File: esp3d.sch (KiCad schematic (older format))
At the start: 12 parts, among them J1 PROG, U1 LM1117-3.3, U2 ESP-12E

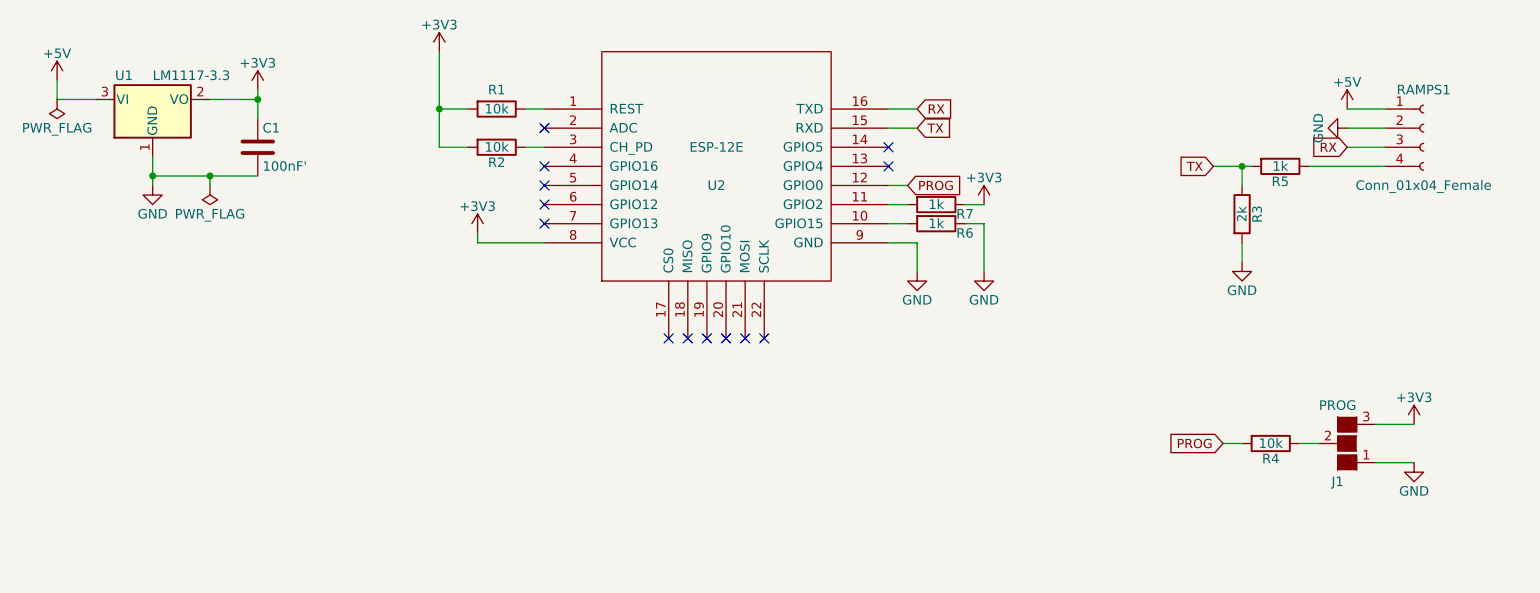
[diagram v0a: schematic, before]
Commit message: Reversed the ramps connector. Removed resistors that may have prevented programming
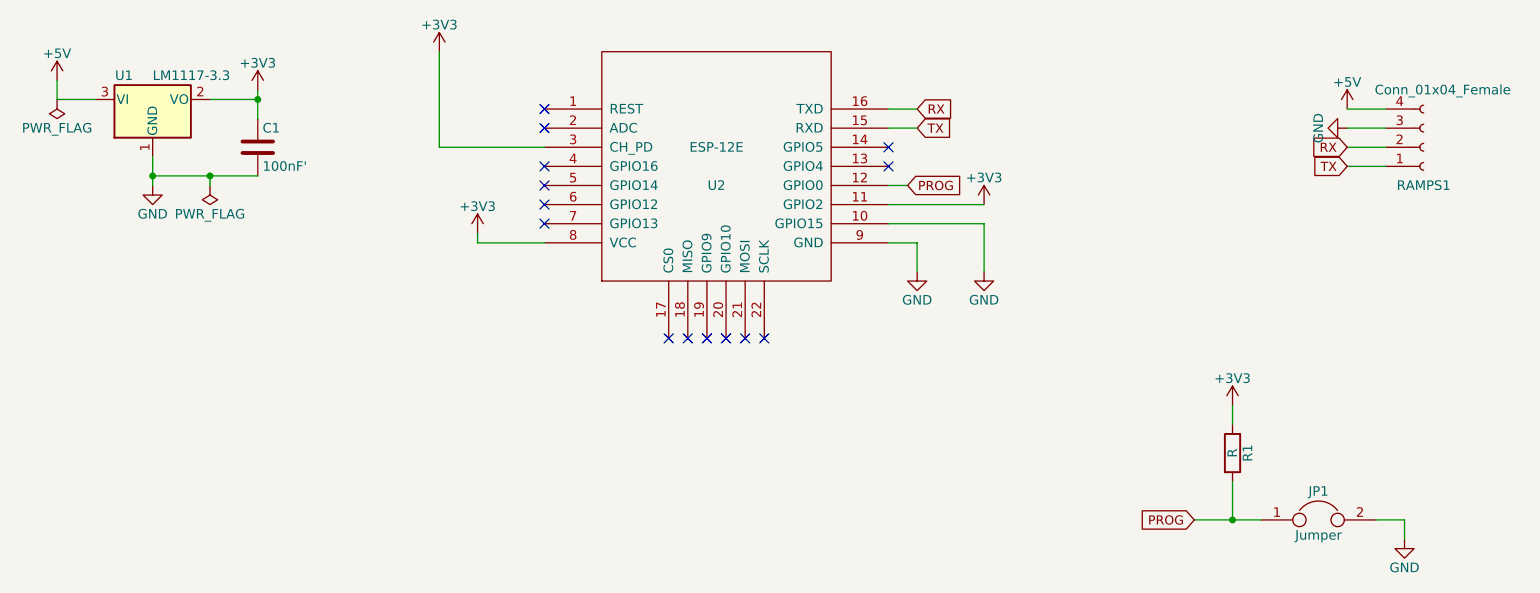
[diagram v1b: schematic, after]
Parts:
- removed J1: PROG, Connectors:GS3, symbol GS3
- removed R2, R4: 10k, Resistors_SMD:R_0805_HandSoldering, symbol R
- removed R3: 2k, Resistors_SMD:R_0805_HandSoldering, symbol R
- removed R5, R6, R7: 1k, Resistors_SMD:R_0805_HandSoldering, symbol R
- added JP1: Jumper, Resistors_Universal:Resistor_SMDuniversal_0805to2512_HandSoldering, symbol Jumper
- R1: value 10k -> R
- U2: footprint RF_Modules:ESP-12E -> ESP8266:ESP-12S_SMD
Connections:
- net +3V3: now also R1.1, U2.11 (GPIO2), U2.3 (CH_PD); no longer R1.2
- net +5V: now also RAMPS1.4 (Pin_4); no longer RAMPS1.1 (Pin_1)
- net GND: now also RAMPS1.3 (Pin_3), U2.10 (GPIO15), JP1.2; no longer RAMPS1.2 (Pin_2)
- net PROG: now also R1.2, JP1.1
- net RX: now also RAMPS1.2 (Pin_2); no longer RAMPS1.3 (Pin_3)
- net TX: now also RAMPS1.1 (Pin_1)
- net at U2.1 (REST): no longer R1.1
- no-connect marks 13 -> 14
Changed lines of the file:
@@
 LIBS:valves
 LIBS:ESP8266
+LIBS:esp3d-cache
 EELAYER 25 0
 EELAYER END
@@
 F 0 "U2" H 5850 3550 50  0000 C CNN
 F 1 "ESP-12E" H 5850 3750 50  0000 C CNN
-F 2 "RF_Modules:ESP-12E" H 5850 3650 50  0001 C CNN
+F 2 "ESP8266:ESP-12S_SMD" H 5850 3650 50  0001 C CNN
 F 3 "" H 5850 3650 50  0001 C CNN
 	1    5850 3650
@@
 L Conn_01x04_Female RAMPS1
 U 1 1 5A19A830
-P 9550 3450
-F 0 "RAMPS1" H 9550 3650 50  0000 C CNN
-F 1 "Conn_01x04_Female" H 9550 3150 50  0000 C CNN
-F 2 "Socket_Strips:Socket_Strip_Straight_1x04_Pitch2.54mm" H 9550 3450 50  0001 C CNN
-F 3 "" H 9550 3450 50  0001 C CNN
-	1    9550 3450
-	1    0    0    -1
+P 9550 3550
+F 0 "RAMPS1" H 9550 3750 50  0000 C CNN
+F 1 "Conn_01x04_Female" H 9650 3250 50  0000 C CNN
+F 2 "Socket_Strips:Socket_Strip_Straight_1x04_Pitch2.54mm" H 9550 3550 50  0001 C CNN
+F 3 "" H 9550 3550 50  0001 C CNN
+	1    9550 3550
+	1    0    0    1
 $EndComp
 $Comp
@@
 Text GLabel 9150 3550 0    48   Input ~ 0
 RX
-Text GLabel 8450 3650 0    48   Input ~ 0
+Text GLabel 9150 3650 0    48   Input ~ 0
 TX
 $Comp
@@
 	1    0    0    -1
 $EndComp
-$Comp
-L GS3 J1
-U 1 1 5A19AC67
-P 9150 5100
-F 0 "J1" H 9200 5300 50  0000 C CNN
-F 1 "PROG" H 9200 4901 50  0000 C CNN
-F 2 "Connectors:GS3" V 9238 5026 50  0001 C CNN
-F 3 "" H 9150 5100 50  0001 C CNN
-	1    9150 5100
-	-1   0    0    1
-$EndComp
 Text GLabel 6850 3750 2    48   Input ~ 0
 PROG
-Text GLabel 8500 5100 0    48   Input ~ 0
+Text GLabel 8350 5500 0    48   Input ~ 0
 PROG
 $Comp
 L +3V3 #PWR010
 U 1 1 5A19AD87
-P 9500 5000
-F 0 "#PWR010" H 9500 4850 50  0001 C CNN
-F 1 "+3V3" H 9500 5140 50  0000 C CNN
-F 2 "" H 9500 5000 50  0001 C CNN
-F 3 "" H 9500 5000 50  0001 C CNN
-	1    9500 5000
+P 8550 4900
+F 0 "#PWR010" H 8550 4750 50  0001 C CNN
+F 1 "+3V3" H 8550 5040 50  0000 C CNN
+F 2 "" H 8550 4900 50  0001 C CNN
+F 3 "" H 8550 4900 50  0001 C CNN
+	1    8550 4900
 	1    0    0    -1
 $EndComp
@@
 L GND #PWR011
 U 1 1 5A19AD9E
-P 9500 5200
-F 0 "#PWR011" H 9500 4950 50  0001 C CNN
-F 1 "GND" H 9500 5050 50  0000 C CNN
-F 2 "" H 9500 5200 50  0001 C CNN
-F 3 "" H 9500 5200 50  0001 C CNN
-	1    9500 5200
+P 9450 5600
+F 0 "#PWR011" H 9450 5350 50  0001 C CNN
+F 1 "GND" H 9450 5450 50  0000 C CNN
+F 2 "" H 9450 5600 50  0001 C CNN
+F 3 "" H 9450 5600 50  0001 C CNN
+	1    9450 5600
 	1    0    0    -1
 $EndComp
@@
 Text GLabel 6900 3450 2    48   Input ~ 0
 TX
-$Comp
-L R R5
-U 1 1 5A19B33E
-P 8800 3650
-F 0 "R5" V 8880 3650 50  0000 C CNN
-F 1 "1k" V 8800 3650 50  0000 C CNN
-F 2 "Resistors_SMD:R_0805_HandSoldering" V 8730 3650 50  0001 C CNN
-F 3 "" H 8800 3650 50  0001 C CNN
-	1    8800 3650
-	0    1    1    0
-$EndComp
-$Comp
-L R R3
-U 1 1 5A19B407
-P 8600 3900
-F 0 "R3" V 8680 3900 50  0000 C CNN
-F 1 "2k" V 8600 3900 50  0000 C CNN
-F 2 "Resistors_SMD:R_0805_HandSoldering" V 8530 3900 50  0001 C CNN
-F 3 "" H 8600 3900 50  0001 C CNN
-	1    8600 3900
-	1    0    0    -1
-$EndComp
 Wire Wire Line
 	2400 3200 2400 3300
@@
 	9150 3550 9350 3550
 Wire Wire Line
-	8950 3650 9350 3650
-Wire Wire Line
 	2900 3750 2900 3600
 Wire Wire Line
 	6750 3750 6850 3750
 Wire Wire Line
-	8900 5100 9000 5100
-Wire Wire Line
-	9300 5200 9500 5200
-Wire Wire Line
-	9300 5000 9500 5000
-Wire Wire Line
 	6750 3350 6900 3350
 Wire Wire Line
 	6750 3450 6900 3450
-Wire Wire Line
-	8600 3750 8600 3650
-Wire Wire Line
-	8450 3650 8650 3650
-Connection ~ 8600 3650
-$Comp
-L GND #PWR012
-U 1 1 5A19B55C
-P 8600 4150
-F 0 "#PWR012" H 8600 3900 50  0001 C CNN
-F 1 "GND" H 8600 4000 50  0000 C CNN
-F 2 "" H 8600 4150 50  0001 C CNN
-F 3 "" H 8600 4150 50  0001 C CNN
-	1    8600 4150
-	1    0    0    -1
-$EndComp
-Wire Wire Line
-	8600 4150 8600 4050
 Wire Wire Line
 	2900 3700 3450 3700
 Connection ~ 2900 3700
 Connection ~ 3450 3300
-$Comp
-L R R1
-U 1 1 5A19B8DB
-P 4700 3350
-F 0 "R1" V 4600 3350 50  0000 C CNN
-F 1 "10k" V 4700 3350 50  0000 C CNN
-F 2 "Resistors_SMD:R_0805_HandSoldering" V 4630 3350 50  0001 C CNN
-F 3 "" H 4700 3350 50  0001 C CNN
-	1    4700 3350
-	0    1    1    0
-$EndComp
-$Comp
-L R R2
-U 1 1 5A19B96A
-P 4700 3550
-F 0 "R2" V 4780 3550 50  0000 C CNN
-F 1 "10k" V 4700 3550 50  0000 C CNN
-F 2 "Resistors_SMD:R_0805_HandSoldering" V 4630 3550 50  0001 C CNN
-F 3 "" H 4700 3550 50  0001 C CNN
-	1    4700 3550
-	0    1    1    0
-$EndComp
-Wire Wire Line
-	4850 3350 4950 3350
-Wire Wire Line
-	4550 3350 4400 3350
 Wire Wire Line
 	4400 3050 4400 3550
-Connection ~ 4400 3350
-$Comp
-L R R4
-U 1 1 5A19BE58
-P 8750 5100
-F 0 "R4" V 8830 5100 50  0000 C CNN
-F 1 "10k" V 8750 5100 50  0000 C CNN
-F 2 "Resistors_SMD:R_0805_HandSoldering" V 8680 5100 50  0001 C CNN
-F 3 "" H 8750 5100 50  0001 C CNN
-	1    8750 5100
-	0    1    1    0
-$EndComp
-Wire Wire Line
-	8500 5100 8600 5100
-Wire Wire Line
-	4850 3550 4950 3550
-Wire Wire Line
-	4400 3550 4550 3550
+Wire Wire Line
+	4400 3550 4950 3550
 NoConn ~ 4950 3950
 NoConn ~ 4950 3850
@@
 NoConn ~ 6100 4550
 $Comp
-L PWR_FLAG #FLG013
+L PWR_FLAG #FLG012
 U 1 1 5A19CD71
 P 2400 3300
-F 0 "#FLG013" H 2400 3375 50  0001 C CNN
+F 0 "#FLG012" H 2400 3375 50  0001 C CNN
 F 1 "PWR_FLAG" H 2400 3450 50  0000 C CNN
 F 2 "" H 2400 3300 50  0001 C CNN
@@
 $EndComp
 $Comp
-L PWR_FLAG #FLG014
+L PWR_FLAG #FLG013
 U 1 1 5A19CEAF
 P 3200 3750
-F 0 "#FLG014" H 3200 3825 50  0001 C CNN
+F 0 "#FLG013" H 3200 3825 50  0001 C CNN
 F 1 "PWR_FLAG" H 3200 3900 50  0000 C CNN
 F 2 "" H 3200 3750 50  0001 C CNN
@@
 Wire Wire Line
 	6900 4050 6900 4200
-$Comp
-L R R6
-U 1 1 5A19D28F
-P 7000 3950
-F 0 "R6" V 7050 4100 50  0000 C CNN
-F 1 "1k" V 7000 3950 50  0000 C CNN
-F 2 "Resistors_SMD:R_0805_HandSoldering" V 6930 3950 50  0001 C CNN
-F 3 "" H 7000 3950 50  0001 C CNN
-	1    7000 3950
-	0    1    1    0
-$EndComp
-Wire Wire Line
-	6750 3950 6850 3950
-Wire Wire Line
-	7150 3950 7250 3950
+Wire Wire Line
+	6750 3950 7250 3950
 Wire Wire Line
 	7250 3950 7250 4200
 $Comp
-L GND #PWR015
+L GND #PWR014
 U 1 1 5A19D3A8
 P 7250 4200
-F 0 "#PWR015" H 7250 3950 50  0001 C CNN
+F 0 "#PWR014" H 7250 3950 50  0001 C CNN
 F 1 "GND" H 7250 4050 50  0000 C CNN
 F 2 "" H 7250 4200 50  0001 C CNN
@@
 	1    0    0    -1
 $EndComp
-$Comp
-L R R7
-U 1 1 5A19D586
-P 7000 3850
-F 0 "R7" V 7050 4000 50  0000 C CNN
-F 1 "1k" V 7000 3850 50  0000 C CNN
-F 2 "Resistors_SMD:R_0805_HandSoldering" V 6930 3850 50  0001 C CNN
-F 3 "" H 7000 3850 50  0001 C CNN
-	1    7000 3850
-	0    1    1    0
-$EndComp
-Wire Wire Line
-	7150 3850 7250 3850
-Wire Wire Line
-	6750 3850 6850 3850
+Wire Wire Line
+	6750 3850 7250 3850
+NoConn ~ 4950 3350
+Wire Wire Line
+	9150 3650 9350 3650
+$Comp
+L R R1
+U 1 1 5A246878
+P 8550 5150
+F 0 "R1" V 8630 5150 50  0000 C CNN
+F 1 "R" V 8550 5150 50  0000 C CNN
+F 2 "Resistors_SMD:R_0805_HandSoldering" V 8480 5150 50  0001 C CNN
+F 3 "" H 8550 5150 50  0001 C CNN
+	1    8550 5150
+	1    0    0    -1
+$EndComp
+$Comp
+L Jumper JP1
+U 1 1 5A2468CB
+P 9000 5500
+F 0 "JP1" H 9000 5650 50  0000 C CNN
+F 1 "Jumper" H 9000 5420 50  0000 C CNN
+F 2 "Resistors_Universal:Resistor_SMDuniversal_0805to2512_HandSoldering" H 9000 5500 50  0001 C CNN
+F 3 "" H 9000 5500 50  0001 C CNN
+	1    9000 5500
+	1    0    0    -1
+$EndComp
+Wire Wire Line
+	8550 5000 8550 4900
+Wire Wire Line
+	8350 5500 8700 5500
+Wire Wire Line
+	8550 5300 8550 5500
+Connection ~ 8550 5500
+Wire Wire Line
+	9300 5500 9450 5500
+Wire Wire Line
+	9450 5500 9450 5600
 $EndSCHEMATC
